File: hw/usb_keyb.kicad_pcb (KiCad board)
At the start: 4 copper layers, 99.1 x 48.3 mm, 107 parts, among them J10 SPI, J11 RMII, J12 PS2, J13 OUT_JMP, J14 MTX_JMP, J2 Micro_SD_Card, J3 USB_1, J4 ZX-BUS, J7 I2C, J8 UART, J9 PROG, SW1 RESET, SW2 OUTPUT, SW3 MATRIX, U1 LM3671MF, U2 STM32F407VETx, U3 STMPS2161STR, U4 NUP4201MR6, U5 74LS245, Y1 8MHz

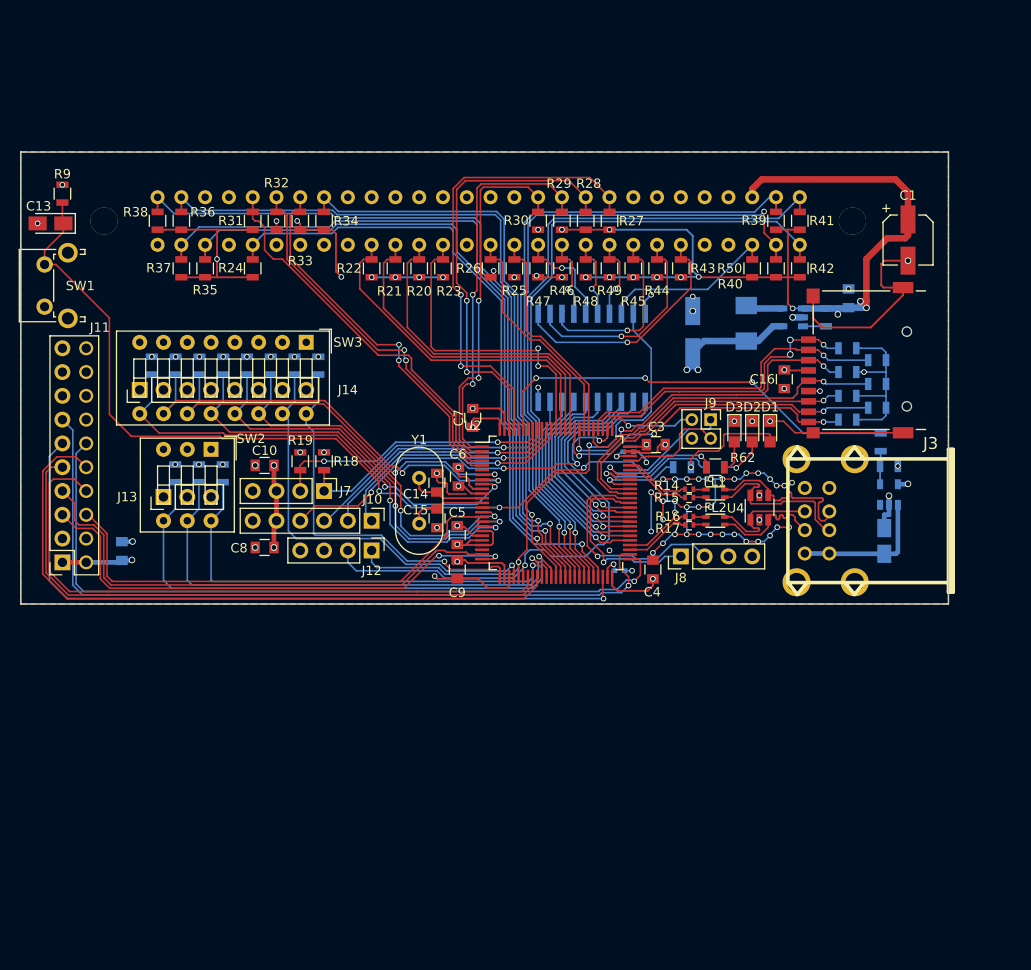
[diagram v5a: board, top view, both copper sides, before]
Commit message: Обновление трассировки платы - версия для производства
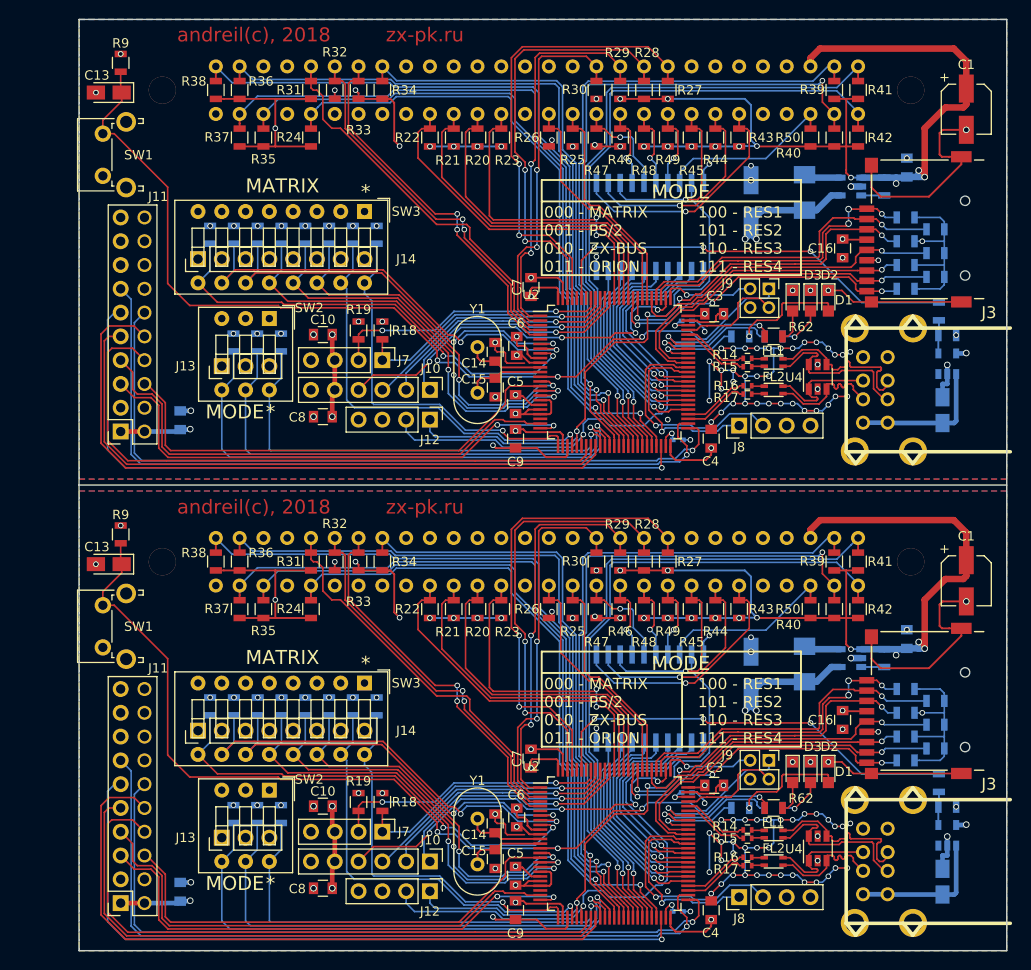
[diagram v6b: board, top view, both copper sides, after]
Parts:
- added C1: 100u, Capacitors_SMD:CP_Elec_5x5.7, F.Cu at (197.5, 55.8)
- added C10: 100n, Capacitors_SMD:C_0805, F.Cu at (128.8, 79.8)
- added C11: 100n, Capacitors_SMD:C_0805, B.Cu at (113.5, 89.0)
- added C12: 100n, Capacitors_SMD:C_0805, B.Cu at (191.1, 62.0)
- added C13: 10uF, Capacitors_Tantalum_SMD:CP_Tantalum_Case-A_EIA-3216-18_Reflow, F.Cu at (105.9, 54.0)
- added C14: 22pF, Capacitors_SMD:C_0805, F.Cu at (147.2, 81.7)
- added C15: 22pF, Capacitors_SMD:C_0805, F.Cu at (147.2, 85.5)
- added C16: 100n, Capacitors_SMD:C_0805, F.Cu at (184.3, 70.6)
- added C17: 4,7uF, Capacitors_Tantalum_SMD:CP_Tantalum_Case-A_EIA-3216-18_Reflow, B.Cu at (194.9, 87.9)
- added C18: 2,2u, Capacitors_SMD:C_0402, B.Cu at (167.6, 78.4)
- added C19: 2,2u, Capacitors_SMD:C_0402, B.Cu at (166.7, 91.1)
- added C2: 100u, Capacitors_SMD:CP_Elec_5x5.7, B.Cu at (174.5, 65.5)
- added C3: 100n, Capacitors_SMD:C_0805, F.Cu at (170.6, 77.6)
- added C4: 100n, Capacitors_SMD:C_0805, F.Cu at (170.2, 90.9)
- added C5: 100n, Capacitors_SMD:C_0805, F.Cu at (149.4, 87.2)
- added C6: 100n, Capacitors_SMD:C_0805, F.Cu at (149.5, 81.0)
- added C7: 100n, Capacitors_SMD:C_0805, F.Cu at (151.0, 74.7)
- added C8: 100n, Capacitors_SMD:C_0805, F.Cu at (128.8, 88.6)
- added C9: 100n, Capacitors_SMD:C_0805, F.Cu at (149.4, 90.9)
- added D1: L1, LEDs:LED_0805, F.Cu at (182.8, 76.2)
- added D2: L2, LEDs:LED_0805, F.Cu at (180.8, 76.2)
- added D3: ERR, LEDs:LED_0805, F.Cu at (178.9, 76.2)
- added FL1: DLW21SN371SQ2, Projects:DLW21S, F.Cu at (176.9, 82.8)
- added FL2: DLW21SN371SQ2, Projects:DLW21S, F.Cu at (176.9, 85.7)
- added J10: SPI, Socket_Strips:Socket_Strip_Straight_1x06_Pitch2.54mm, F.Cu at (140.2, 85.7)
- added J11: RMII, Socket_Strips:Socket_Strip_Straight_2x10_Pitch2.54mm, F.Cu at (107.2, 90.2)
- added J12: PS2, Socket_Strips:Socket_Strip_Straight_1x04_Pitch2.54mm, F.Cu at (140.2, 88.9)
- added J13: OUT_JMP, Pin_Headers:Pin_Header_Straight_1x03_Pitch2.54mm, F.Cu at (118.0, 83.2)
- added J14: MTX_JMP, Pin_Headers:Pin_Header_Straight_1x08_Pitch2.54mm, F.Cu at (115.4, 71.8)
- added J2: Micro_SD_Card, Projects:Conn_uSDcard, F.Cu at (197.4, 68.6)
- added J3: USB_1, Projects:conn_usb_Ax2, F.Cu at (193.5, 85.7)
- added J4: ZX-BUS, Projects:Socket_DIN41612-CaseC1-AB-Female-56Pin-2rows, B.Cu at (146.6, 53.7)
- added J7: I2C, Socket_Strips:Socket_Strip_Straight_1x04_Pitch2.54mm, F.Cu at (135.1, 82.5)
- added J8: UART, Socket_Strips:Socket_Strip_Straight_1x04_Pitch2.54mm, F.Cu at (173.2, 89.5)
- added J9: PROG, Socket_Strips:Socket_Strip_Straight_2x02_Pitch2.00mm, F.Cu at (176.4, 74.9)
- added L1: 2.2µH, Inductors_SMD:L_Vishay_IHLP-1616, B.Cu at (180.2, 64.6)
- added R1: 10k, Resistors_SMD:R_0805, B.Cu at (188.7, 64.0)
- added R10: 0, Resistors_SMD:R_0805, B.Cu at (194.6, 77.3)
- added R11: 10k, Resistors_SMD:R_0805, B.Cu at (195.5, 79.9)
- added R12: 10k, Resistors_SMD:R_0805, B.Cu at (173.4, 80.0)
- added R13: 10k, Resistors_SMD:R_0805, B.Cu at (176.9, 80.0)
- added R14: 22, Resistors_SMD:R_0402, F.Cu at (174.1, 82.4)
- added R15: 22, Resistors_SMD:R_0402, F.Cu at (174.1, 83.2)
- added R16: 22, Resistors_SMD:R_0402, F.Cu at (174.1, 85.3)
- added R17: 22, Resistors_SMD:R_0402, F.Cu at (174.1, 86.2)
- added R18: 10k, Resistors_SMD:R_0805, F.Cu at (135.1, 79.4)
- added R19: 10k, Resistors_SMD:R_0805, F.Cu at (132.6, 79.4)
- added R2: 10k, Resistors_SMD:R_0805, B.Cu at (191.0, 72.4)
- added R20: 10k, Resistors_SMD:R_0805, F.Cu at (145.3, 58.8)
- added R21: 10k, Resistors_SMD:R_0805, F.Cu at (142.7, 58.8)
- added R22: 10k, Resistors_SMD:R_0805, F.Cu at (140.2, 58.8)
- added R23: 10k, Resistors_SMD:R_0805, F.Cu at (147.8, 58.8)
- added R24: 10k, Resistors_SMD:R_0805, F.Cu at (127.5, 58.8)
- added R25: 10k, Resistors_SMD:R_0805, F.Cu at (155.4, 58.8)
- added R26: 10k, Resistors_SMD:R_0805, F.Cu at (152.9, 58.8)
- added R27: 10k, Resistors_SMD:R_0805, F.Cu at (165.6, 53.7)
- added R28: 10k, Resistors_SMD:R_0805, F.Cu at (163.1, 53.7)
- added R29: 10k, Resistors_SMD:R_0805, F.Cu at (160.5, 53.7)
- added R3: 10k, Resistors_SMD:R_0805, B.Cu at (194.2, 73.7)
- added R30: 10k, Resistors_SMD:R_0805, F.Cu at (158.0, 53.7)
- added R31: 10k, Resistors_SMD:R_0805, F.Cu at (127.5, 53.7)
- added R32: 10k, Resistors_SMD:R_0805, F.Cu at (130.0, 53.7)
- added R33: 10k, Resistors_SMD:R_0805, F.Cu at (132.6, 53.7)
- added R34: 10k, Resistors_SMD:R_0805, F.Cu at (135.1, 53.7)
- added R35: 10k, Resistors_SMD:R_0805, F.Cu at (122.4, 58.8)
- added R36: 10k, Resistors_SMD:R_0805, F.Cu at (119.9, 53.7)
- added R37: 10k, Resistors_SMD:R_0805, F.Cu at (119.9, 58.8)
- added R38: 10k, Resistors_SMD:R_0805, F.Cu at (117.3, 53.7)
- added R39: 10k, Resistors_SMD:R_0805, F.Cu at (183.4, 53.7)
- added R4: 10k, Resistors_SMD:R_0805, B.Cu at (191.0, 67.3)
- added R40: 10k, Resistors_SMD:R_0805, F.Cu at (183.4, 58.8)
- added R41: 10k, Resistors_SMD:R_0805, F.Cu at (185.9, 53.7)
- added R42: 10k, Resistors_SMD:R_0805, F.Cu at (185.9, 58.8)
- added R43: 10k, Resistors_SMD:R_0805, F.Cu at (173.2, 58.8)
- added R44: 10k, Resistors_SMD:R_0805, F.Cu at (170.7, 58.8)
- added R45: 10k, Resistors_SMD:R_0805, F.Cu at (168.1, 58.8)
- added R46: 10k, Resistors_SMD:R_0805, F.Cu at (160.5, 58.8)
- added R47: 10k, Resistors_SMD:R_0805, F.Cu at (158.0, 58.8)
- added R48: 10k, Resistors_SMD:R_0805, F.Cu at (163.1, 58.8)
- added R49: 10k, Resistors_SMD:R_0805, F.Cu at (165.6, 58.8)
- added R5: 10k, Resistors_SMD:R_0805, B.Cu at (194.2, 68.6)
- added R50: 10k, Resistors_SMD:R_0805, F.Cu at (180.8, 58.8)
- added R51: 10k, Resistors_SMD:R_0805, B.Cu at (124.3, 80.7)
- added R52: 10k, Resistors_SMD:R_0805, B.Cu at (121.8, 80.7)
- added R53: 10k, Resistors_SMD:R_0805, B.Cu at (119.2, 80.7)
- added R54: 10k, Resistors_SMD:R_0805, B.Cu at (134.5, 69.2)
- added R55: 10k, Resistors_SMD:R_0805, B.Cu at (132.0, 69.2)
- added R56: 10k, Resistors_SMD:R_0805, B.Cu at (129.4, 69.2)
- added R57: 10k, Resistors_SMD:R_0805, B.Cu at (126.9, 69.2)
- added R58: 10k, Resistors_SMD:R_0805, B.Cu at (124.4, 69.2)
- added R59: 10k, Resistors_SMD:R_0805, B.Cu at (121.8, 69.2)
- added R6: 10k, Resistors_SMD:R_0805, B.Cu at (191.0, 69.8)
- added R60: 10k, Resistors_SMD:R_0805, B.Cu at (119.3, 69.2)
- added R61: 10k, Resistors_SMD:R_0805, B.Cu at (116.7, 69.2)
- added R62: 10k, Resistors_SMD:R_0805, F.Cu at (176.9, 80.0)
- added R7: 10k, Resistors_SMD:R_0805, B.Cu at (194.2, 71.1)
- added R8: 10k, Resistors_SMD:R_0805, B.Cu at (191.0, 74.9)
- added R9: 10k, Resistors_SMD:R_0805, F.Cu at (107.2, 50.8)
- added SW1: RESET, Buttons_Switches_THT:SW_Tactile_SPST_Angled_PTS645Vx83-2LFS, F.Cu at (105.3, 62.9)
- added SW2: OUTPUT, Buttons_Switches_THT:SW_DIP_x3_W7.62mm_Slide, F.Cu at (123.1, 78.1)
- added SW3: MATRIX, Buttons_Switches_THT:SW_DIP_x8_W7.62mm_Slide, F.Cu at (133.2, 66.7)
- added U1: LM3671MF, TO_SOT_Packages_SMD:SOT-23-5, B.Cu at (185.2, 64.0)
- added U2: STM32F407VETx, Housings_QFP:LQFP-100_14x14mm_Pitch0.5mm, F.Cu at (159.9, 83.8)
- added U3: STMPS2161STR, TO_SOT_Packages_SMD:SOT-23-5, B.Cu at (195.5, 82.9)
- added U4: NUP4201MR6, TO_SOT_Packages_SMD:TSOT-23-6, F.Cu at (181.6, 84.3)
- added U5: 74LS245, Housings_SOIC:SOIC-20W_7.5x12.8mm_Pitch1.27mm, B.Cu at (163.7, 68.3)
- added Y1: 8MHz, Crystals:Crystal_HC49-4H_Vertical, F.Cu at (145.3, 81.2)
- moved C1 36.9 mm to (197.5, 106.1)
- moved C10 36.9 mm to (128.8, 130.2)
- moved C12 36.9 mm to (191.1, 112.3)
- moved C13 36.9 mm to (105.9, 104.3)
- moved C14 36.9 mm to (147.2, 132.0)
- moved C15 36.9 mm to (147.2, 135.8)
- moved C16 36.9 mm to (184.3, 121.0)
- moved C19 36.9 mm to (166.7, 141.4)
- moved C2 36.9 mm to (174.5, 115.9)
- moved C3 36.9 mm to (170.6, 128.0)
- moved C5 36.9 mm to (149.4, 137.6)
- moved FL1 36.9 mm to (176.9, 133.2)
- moved FL2 36.9 mm to (176.9, 136.1)
- moved J10 36.9 mm to (140.2, 136.1)
- moved J12 36.9 mm to (140.2, 139.3)
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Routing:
- net GND: track 506.3 -> 1012.6 mm, vias 62 -> 124
- net +3V3: track 311.1 -> 622.1 mm, vias 28 -> 56
- net +5V: track 276.8 -> 553.6 mm, vias 27 -> 54
- net RES: track 102.9 -> 205.9 mm, vias 3 -> 6
- net TXD1: track 83.1 -> 166.1 mm, vias 1 -> 2
- net ZA11: track 80.6 -> 161.3 mm, vias 1 -> 2
- net TXD0: track 79.6 -> 159.2 mm, vias 1 -> 2
- net TX_EN: track 77.6 -> 155.9 mm, vias 1 -> 2
- net ZA9: track 78.1 -> 156.4 mm, vias 1 -> 2
- net ZA10: track 76.9 -> 153.9 mm, vias 1 -> 2
- net RXD1: track 72.1 -> 145.0 mm
- net ZA13: track 72.0 -> 144.5 mm, vias 2 -> 4
- net ZA8: track 71.5 -> 143.0 mm, vias 1 -> 2
- net ZA14: track 70.9 -> 141.9 mm, vias 1 -> 2
- net ZA12: track 70.2 -> 140.9 mm, vias 1 -> 2
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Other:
- board size 99.1 x 48.3 mm -> 99.1 x 99.4 mm
- board text added: "*"
- board text added: "000 - MATRIX 001 - PS/2 010 - ZX-BUS 011 - ORION"
- board text added: "100 - RES1 101 - RES2 110 - RES3 111 - RES4"
- board text added: "MATRIX"
- board text added: "MODE"
- board text added: "andreil(c), 2018 zx-pk.ru"
